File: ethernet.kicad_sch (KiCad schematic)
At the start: 29 parts, among them U6 LAN8720A

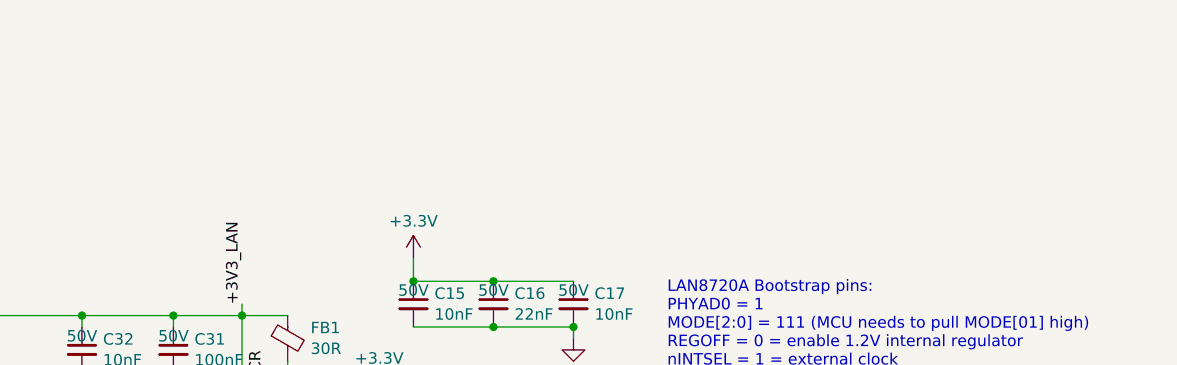
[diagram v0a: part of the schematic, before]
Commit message: updated LED resistor values
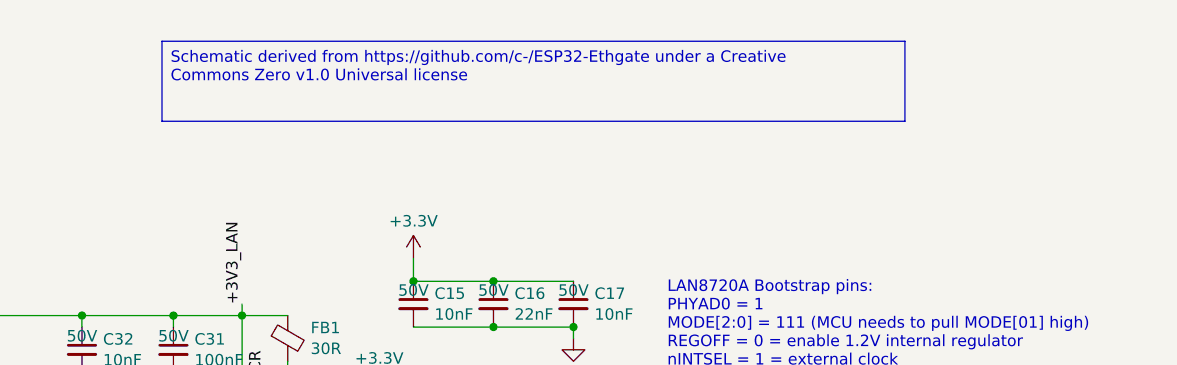
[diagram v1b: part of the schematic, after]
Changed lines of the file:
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@@
+		)
+	)
+	(text_box "Schematic derived from https://github.com/c-/ESP32-Ethgate under a Creative Commons Zero v1.0 Universal license"
+		(exclude_from_sim no)
+		(at 92.71 21.59 0)
+		(size 82.55 8.89)
+		(margins 0.9525 0.9525 0.9525 0.9525)
+		(stroke
+			(width 0)
+			(type solid)
+		)
+		(fill
+			(type none)
+		)
+		(effects
+			(font
+				(size 1.27 1.27)
+			)
+			(justify left top)
 		)
 	)
